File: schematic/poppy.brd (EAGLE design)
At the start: 31 x 51.9 mm, 16 parts, among them Q1 8MHz, U1 ATUSB, U2 MBI5039

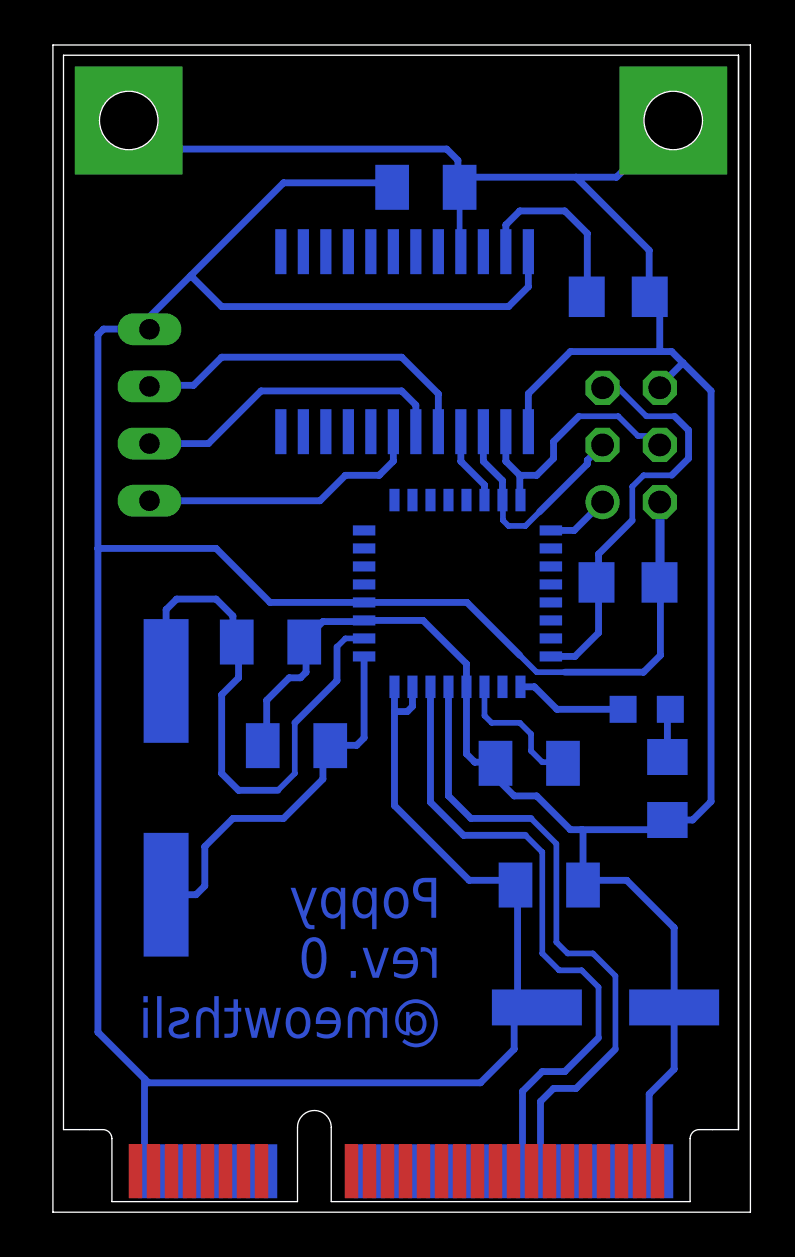
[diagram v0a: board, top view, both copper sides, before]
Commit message: atmega16u4 tqfp44 added
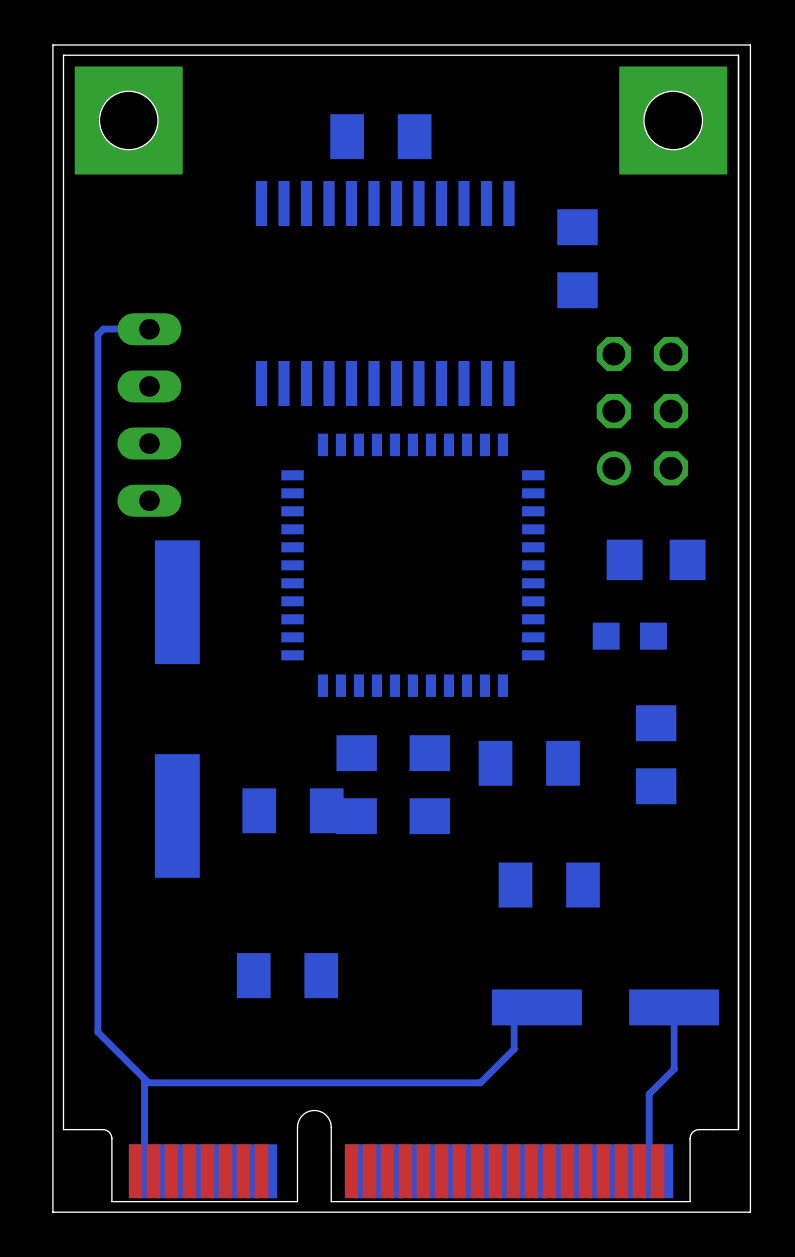
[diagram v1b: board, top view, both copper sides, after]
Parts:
- removed U1: ATUSB, at90usb:VQFP32
- removed U2: MBI5039, _LedDrivers:SOP24-300-1.00
- added R4, R5: 22, resistor:R3216
- added U$1: ATMEGA16U4TQFP44, p1poppy:ATMEGA16U4_TQFP
- added U$2: MBI5030GFSOP-24, p1poppy:_LEDDRIVERS_SOP24-300-1.00
- moved C3 10.2 mm to (9.93, 10.0), turned to 180 degrees
- moved C4 7.57 mm to (10.2, 17.3)
- moved Q1 3.54 mm to (5.03, 21.9)
- moved LED1 3.34 mm to (25.1, 25.1)
- moved C6 3.01 mm to (14.1, 47.3)
- moved R3 2.48 mm to (22.8, 41.9), turned to 270 degrees
- moved R1 1.60 mm to (26.3, 28.5)
- moved ISP 1.58 mm to (25.7, 35.1)
- moved R2 1.58 mm to (26.3, 19.8)
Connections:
- new net CLK0: U$1.32, U$2.21
- new net N$10: R5.1, U$1.3
- new net N$9: R4.1, U$1.4
- net D+: now also R4.2; no longer U1.29
- net D-: now also R5.2; no longer U1.30
- net GND: now also U$1.15, U$1.23, U$1.35, U$1.42, U$1.43, U$1.5, U$2.1; no longer U1.28, U1.3, U2.1, U2.21
- net LATCH: now also U$1.8, U$2.4; no longer U1.14, U2.4
- net MISO: now also U$1.11; no longer U1.17
- net MOSI/DATA: now also U$1.10, U$2.2; no longer U1.16, U2.2
- net N$1: now also U$1.37; no longer U1.25
- net N$2: now also U$2.23; no longer U2.23
- net N$3: now also U$2.5; no longer U2.5
- net N$4: now also U$1.6; no longer U1.27
- net N$5: now also U$2.6; no longer U2.6
- net N$6: now also U$2.7; no longer U2.7
- net RESET: now also U$1.13; no longer U1.24
- net SCK: now also U$1.9, U$2.3; no longer U1.15, U2.3
- net VCC: now also U$1.14, U$1.2, U$1.24, U$1.34, U$1.44, U$1.7, U$2.24; no longer U1.31, U1.32, U1.4, U2.24
- net XTAL1: now also U$1.17; no longer U1.1
- net XTAL2: now also U$1.16; no longer U1.2
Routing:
- net GND: track 124.6 -> 10.8 mm
- net VCC: track 146.6 -> 61.4 mm
- net D-: track 28.8 -> 0.00 mm
- net D+: track 28.8 -> 0.00 mm
- net XTAL2: track 25.7 -> 0.00 mm
- net RESET: track 18.8 -> 0.00 mm
- net XTAL1: track 17.0 -> 0.00 mm
- net N$3: track 15.7 -> 0.00 mm
- net N$5: track 14.3 -> 0.00 mm
- net N$6: track 12.9 -> 0.00 mm
- net MOSI/DATA: track 11.6 -> 0.00 mm
- net SCK: track 10.5 -> 0.00 mm
- net N$2: track 8.31 -> 0.00 mm
- net N$4: track 6.19 -> 0.00 mm
- net N$1: track 4.97 -> 0.00 mm
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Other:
- board text removed: "Poppy rev. 0 @meowthsli"

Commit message: routed everything
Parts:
- removed U$1: ATMEGA16U4TQFP44, p1poppy:ATMEGA16U4_TQFP
- removed U$2: MBI5030GFSOP-24, p1poppy:_LEDDRIVERS_SOP24-300-1.00
- added U1: ATMEGA16U4TQFP44, p1poppy:ATMEGA16U4_TQFP
- added U2: MBI5030GFSOP-24, p1poppy:_LEDDRIVERS_SOP24-300-1.00
- R1: value 10k -> 22; device resistor:R3216 -> resistor:R1206
- R2: value 1k -> 22; device resistor:R3216 -> resistor:R1206
- R3: value 1k -> 10k; device resistor:R3216 -> resistor:R1206
- R4, R5: value 22 -> 1k; device resistor:R3216 -> resistor:R1206
- moved ISP 32.9 mm to (4.30, 10.2), turned to 270 degrees
- moved R5 26.1 mm to (26.2, 42.6), turned to 90 degrees
- moved R3 21.9 mm to (10.9, 23.5), turned to 0 degrees
- moved R4 19.9 mm to (26.9, 32.7)
- moved C3 19.8 mm to (9.66, 29.8), turned to 270 degrees
- moved R1 13.2 mm to (23.8, 15.5), turned to 270 degrees
- moved LED1 12.7 mm to (26.9, 37.6), turned to 0 degrees
- moved C4 12.1 mm to (7.09, 29.1), turned to 270 degrees
- moved C6 9.59 mm to (23.3, 44.7), turned to 270 degrees
- moved C1 7.47 mm to (21.8, 21.5), turned to 0 degrees
- moved R2 5.58 mm to (21.5, 17.0), turned to 270 degrees
- moved LED2 4.28 mm to (3.29, 39.2)
- moved C5 3.51 mm to (17.4, 20.7), turned to 270 degrees
- moved Q1 2.97 mm to (3.47, 24.4), turned to 270 degrees
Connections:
- new net DCLK: U1.28, U2.3
- new net SDI: U1.29, U2.2
- net CLK0: now also U1.32, U2.21; no longer U$1.32, U$2.21
- net D+: now also R1.2; no longer R4.2
- net D-: now also R2.2; no longer R5.2
- net GND: now also LED1.C, R5.1, U1.15, U1.23, U1.35, U1.42, U1.43, U1.5, U2.1; no longer R2.1, R3.1, U$1.15, U$1.23, U$1.35, U$1.42, U$1.43, U$1.5, U$2.1
- net LATCH: now also U1.30, U2.4; no longer U$1.8, U$2.4
- net MISO: now also U1.11; no longer U$1.11
- net MOSI/DATA: now also U1.10; no longer U$1.10, U$2.2
- net N$1: now also R4.2, U1.37; no longer LED1.A, U$1.37
- net N$10: now also R2.1, U1.3; no longer R5.1, U$1.3
- net N$2: now also R5.2, U2.23; no longer R3.2, U$2.23
- net N$3: now also U2.5; no longer U$2.5
- net N$4: now also U1.6; no longer U$1.6
- net N$5: now also U2.6; no longer U$2.6
- net N$6: now also U2.7; no longer U$2.7
- net N$7: now also LED1.A, R4.1; no longer LED1.C, R2.2
- net N$9: now also R1.1, U1.4; no longer R4.1, U$1.4
- net RESET: now also R3.1, U1.13; no longer R1.1, U$1.13
- net SCK: now also U1.9; no longer U$1.9, U$2.3
- net VCC: now also R3.2, U1.14, U1.2, U1.24, U1.34, U1.44, U1.7, U2.24; no longer R1.2, U$1.14, U$1.2, U$1.24, U$1.34, U$1.44, U$1.7, U$2.24
- net XTAL1: now also U1.17; no longer U$1.17
- net XTAL2: now also U1.16; no longer U$1.16
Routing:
- net GND: track 10.8 -> 177.0 mm, vias 0 -> 4
- net VCC: track 61.4 -> 150.8 mm
- net RESET: track 0.00 -> 24.9 mm, vias 0 -> 2
- net MOSI/DATA: track 0.00 -> 22.4 mm
- net SCK: track 0.00 -> 20.9 mm
- net XTAL2: track 0.00 -> 18.9 mm
- net D-: track 0.00 -> 18.3 mm
- net MISO: track 0.00 -> 17.6 mm
- net N$3: track 0.00 -> 17.2 mm
- net N$5: track 0.00 -> 16.1 mm
- net N$6: track 0.00 -> 15.8 mm
- net D+: track 0.00 -> 15.3 mm
- net CLK0: track 0.00 -> 15.1 mm, vias 0 -> 2
- net XTAL1: track 0.00 -> 13.5 mm
- net N$9: track 0.00 -> 13.2 mm
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
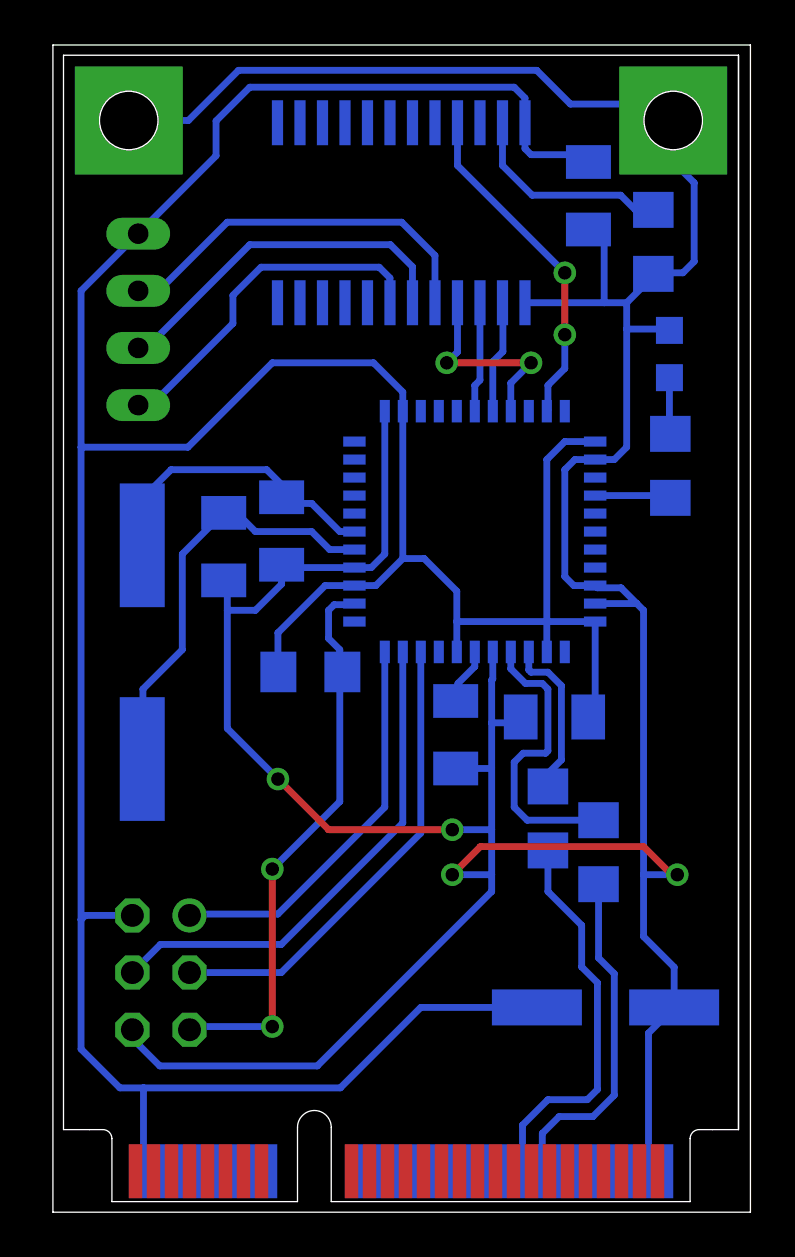
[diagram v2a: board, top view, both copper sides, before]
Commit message: rerouted some parts
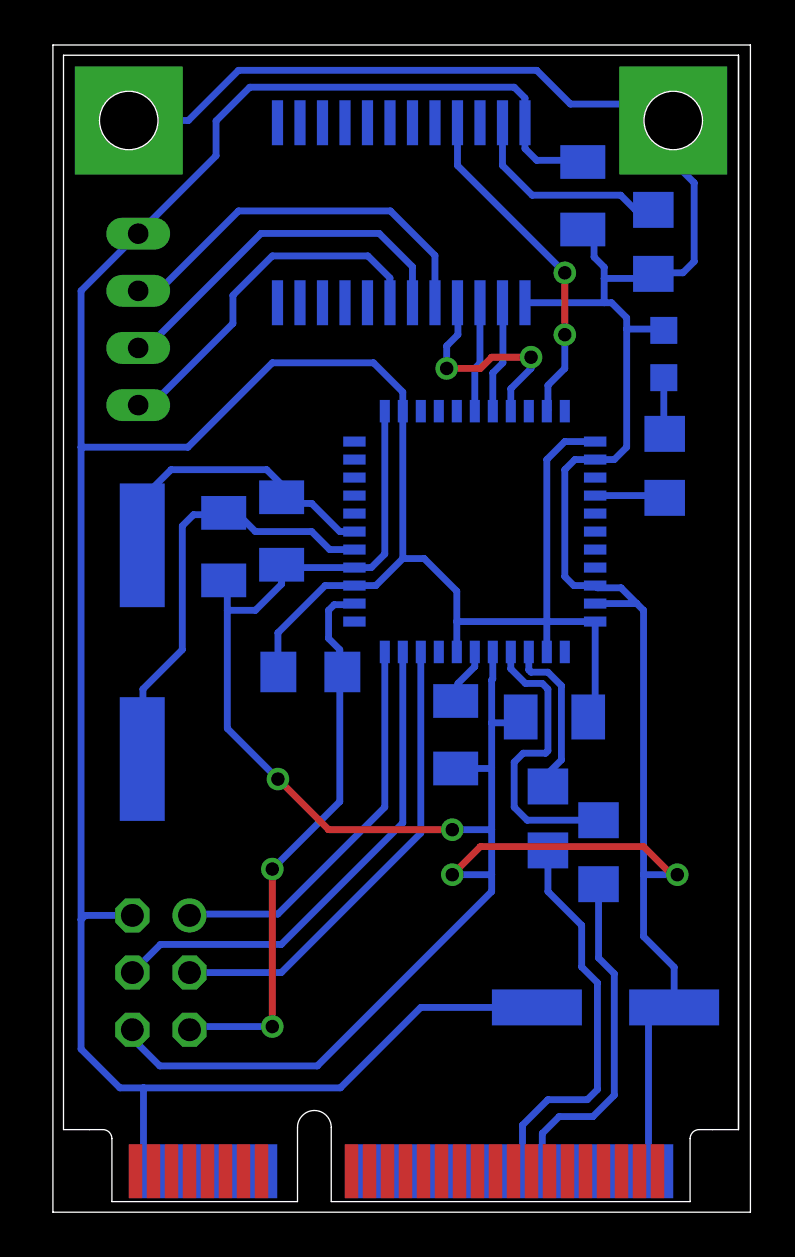
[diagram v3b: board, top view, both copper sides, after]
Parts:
- moved C6 0.25 mm to (23.1, 44.7)
- moved LED1 0.25 mm to (26.6, 37.6)
- moved R4 0.25 mm to (26.7, 32.7)
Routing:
- net GND: track 177.0 -> 178.6 mm
- net XTAL2: track 18.9 -> 19.7 mm
- net LATCH: track 9.14 -> 9.87 mm

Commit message: printed
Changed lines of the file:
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@@
 <grid distance="0.25" unitdist="mm" unit="mm" style="lines" multiple="1" display="no" altdistance="0.1" altunitdist="mm" altunit="mm"/>
 <layers>
-<layer number="1" name="Top" color="4" fill="1" visible="yes" active="yes"/>
+<layer number="1" name="Top" color="4" fill="1" visible="no" active="yes"/>
 <layer number="16" name="Bottom" color="1" fill="1" visible="yes" active="yes"/>
 <layer number="17" name="Pads" color="2" fill="1" visible="yes" active="yes"/>
@@
 <layer number="19" name="Unrouted" color="6" fill="1" visible="yes" active="yes"/>
 <layer number="20" name="Dimension" color="15" fill="1" visible="yes" active="yes"/>
-<layer number="21" name="tPlace" color="7" fill="1" visible="yes" active="yes"/>
-<layer number="22" name="bPlace" color="7" fill="1" visible="yes" active="yes"/>
-<layer number="23" name="tOrigins" color="15" fill="1" visible="yes" active="yes"/>
-<layer number="24" name="bOrigins" color="15" fill="1" visible="yes" active="yes"/>
-<layer number="25" name="tNames" color="7" fill="1" visible="yes" active="yes"/>
-<layer number="26" name="bNames" color="7" fill="1" visible="yes" active="yes"/>
+<layer number="21" name="tPlace" color="7" fill="1" visible="no" active="yes"/>
+<layer number="22" name="bPlace" color="7" fill="1" visible="no" active="yes"/>
+<layer number="23" name="tOrigins" color="15" fill="1" visible="no" active="yes"/>
+<layer number="24" name="bOrigins" color="15" fill="1" visible="no" active="yes"/>
+<layer number="25" name="tNames" color="7" fill="1" visible="no" active="yes"/>
+<layer number="26" name="bNames" color="7" fill="1" visible="no" active="yes"/>
 <layer number="27" name="tValues" color="7" fill="1" visible="no" active="yes"/>
 <layer number="28" name="bValues" color="7" fill="1" visible="no" active="yes"/>
-<layer number="29" name="tStop" color="7" fill="3" visible="yes" active="yes"/>
-<layer number="30" name="bStop" color="7" fill="6" visible="yes" active="yes"/>
+<layer number="29" name="tStop" color="7" fill="3" visible="no" active="yes"/>
+<layer number="30" name="bStop" color="7" fill="6" visible="no" active="yes"/>
 <layer number="31" name="tCream" color="7" fill="4" visible="no" active="yes"/>
 <layer number="32" name="bCream" color="7" fill="5" visible="no" active="yes"/>
 <layer number="33" name="tFinish" color="6" fill="3" visible="yes" active="yes"/>
 <layer number="34" name="bFinish" color="6" fill="6" visible="yes" active="yes"/>
-<layer number="35" name="tGlue" color="7" fill="4" visible="yes" active="yes"/>
+<layer number="35" name="tGlue" color="7" fill="4" visible="no" active="yes"/>
 <layer number="36" name="bGlue" color="7" fill="5" visible="no" active="yes"/>
-<layer number="37" name="tTest" color="7" fill="1" visible="yes" active="yes"/>
-<layer number="38" name="bTest" color="7" fill="1" visible="yes" active="yes"/>
+<layer number="37" name="tTest" color="7" fill="1" visible="no" active="yes"/>
+<layer number="38" name="bTest" color="7" fill="1" visible="no" active="yes"/>
 <layer number="39" name="tKeepout" color="4" fill="11" visible="no" active="yes"/>
 <layer number="40" name="bKeepout" color="1" fill="11" visible="no" active="yes"/>
@@
 <layer number="42" name="bRestrict" color="1" fill="10" visible="no" active="yes"/>
 <layer number="43" name="vRestrict" color="2" fill="10" visible="no" active="yes"/>
-<layer number="44" name="Drills" color="7" fill="1" visible="yes" active="yes"/>
-<layer number="45" name="Holes" color="7" fill="1" visible="yes" active="yes"/>
+<layer number="44" name="Drills" color="7" fill="1" visible="no" active="yes"/>
+<layer number="45" name="Holes" color="7" fill="1" visible="no" active="yes"/>
 <layer number="46" name="Milling" color="3" fill="1" visible="yes" active="yes"/>
-<layer number="47" name="Measures" color="7" fill="1" visible="yes" active="yes"/>
-<layer number="48" name="Document" color="7" fill="1" visible="yes" active="yes"/>
-<layer number="49" name="Reference" color="7" fill="1" visible="yes" active="yes"/>
+<layer number="47" name="Measures" color="7" fill="1" visible="no" active="yes"/>
+<layer number="48" name="Document" color="7" fill="1" visible="no" active="yes"/>
+<layer number="49" name="Reference" color="7" fill="1" visible="no" active="yes"/>
 <layer number="50" name="dxf" color="7" fill="1" visible="no" active="no"/>
-<layer number="51" name="tDocu" color="7" fill="1" visible="yes" active="yes"/>
-<layer number="52" name="bDocu" color="7" fill="1" visible="yes" active="yes"/>
+<layer number="51" name="tDocu" color="7" fill="1" visible="no" active="yes"/>
+<layer number="52" name="bDocu" color="7" fill="1" visible="no" active="yes"/>
 <layer number="53" name="tGND_GNDA" color="7" fill="9" visible="no" active="no"/>
 <layer number="54" name="bGND_GNDA" color="1" fill="9" visible="no" active="no"/>
@@
 <contactref element="U1" pad="4"/>
 <contactref element="R1" pad="1"/>
-<wire x1="19.85" y1="24.4" x2="19.85" y2="23.65" width="0.3048" layer="16"/>
-<wire x1="20.5" y1="20.25" x2="19.75" y2="19.5" width="0" layer="19" extent="1-16"/>
-<wire x1="19.75" y1="19.5" x2="19.75" y2="18" width="0" layer="19" extent="1-16"/>
-<wire x1="19.75" y1="18" x2="20.25" y2="17.5" width="0" layer="19" extent="1-16"/>
-<wire x1="20.25" y1="17.5" x2="23.578" y2="17.5" width="0" layer="19" extent="1-16"/>
-<wire x1="19.85" y1="23.65" x2="20.5" y2="23" width="0.3048" layer="16"/>
-<wire x1="20.5" y1="23" x2="21.25" y2="23" width="0.3048" layer="16"/>
-<wire x1="21.25" y1="23" x2="21.5" y2="22.75" width="0.3048" layer="16"/>
+<wire x1="19.85" y1="24.4" x2="19.85" y2="23.35" width="0.3048" layer="16"/>
 <wire x1="21.5" y1="22.75" x2="21.5" y2="20" width="0.3048" layer="16"/>
-<wire x1="21.5" y1="20.5" x2="21.25" y2="20.25" width="0" layer="19" extent="1-16"/>
-<wire x1="21.25" y1="20.25" x2="20.5" y2="20.25" width="0" layer="19" extent="1-16"/>
 <wire x1="23.75" y1="16.922" x2="20.578" y2="16.922" width="0.3048" layer="16"/>
 <wire x1="20.578" y1="16.922" x2="20" y2="17.5" width="0.3048" layer="16"/>
 <wire x1="20" y1="17.5" x2="20" y2="19.5" width="0.3048" layer="16"/>
 <wire x1="20" y1="19.5" x2="20.4" y2="19.9" width="0.3048" layer="16"/>
-<wire x1="21.5" y1="20.5" x2="21.5" y2="20" width="0" layer="19" extent="1-16"/>
 <wire x1="21.5" y1="20" x2="21.4" y2="19.9" width="0.3048" layer="16"/>
 <wire x1="21.4" y1="19.9" x2="20.4" y2="19.9" width="0.3048" layer="16"/>
+<wire x1="19.85" y1="23.35" x2="20.3" y2="22.9" width="0.3048" layer="16"/>
+<wire x1="20.3" y1="22.9" x2="21.35" y2="22.9" width="0.3048" layer="16"/>
+<wire x1="21.35" y1="22.9" x2="21.5" y2="22.75" width="0.3048" layer="16"/>
 </signal>
 <signal name="N$10">
